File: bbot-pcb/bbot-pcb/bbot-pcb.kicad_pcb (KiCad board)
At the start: 2 copper layers, 72.4 x 56.5 mm, 12 parts, among them U1 HA-552-4P, U2 ADXL335, U3 HA-552-4P, U4 OPENLOG

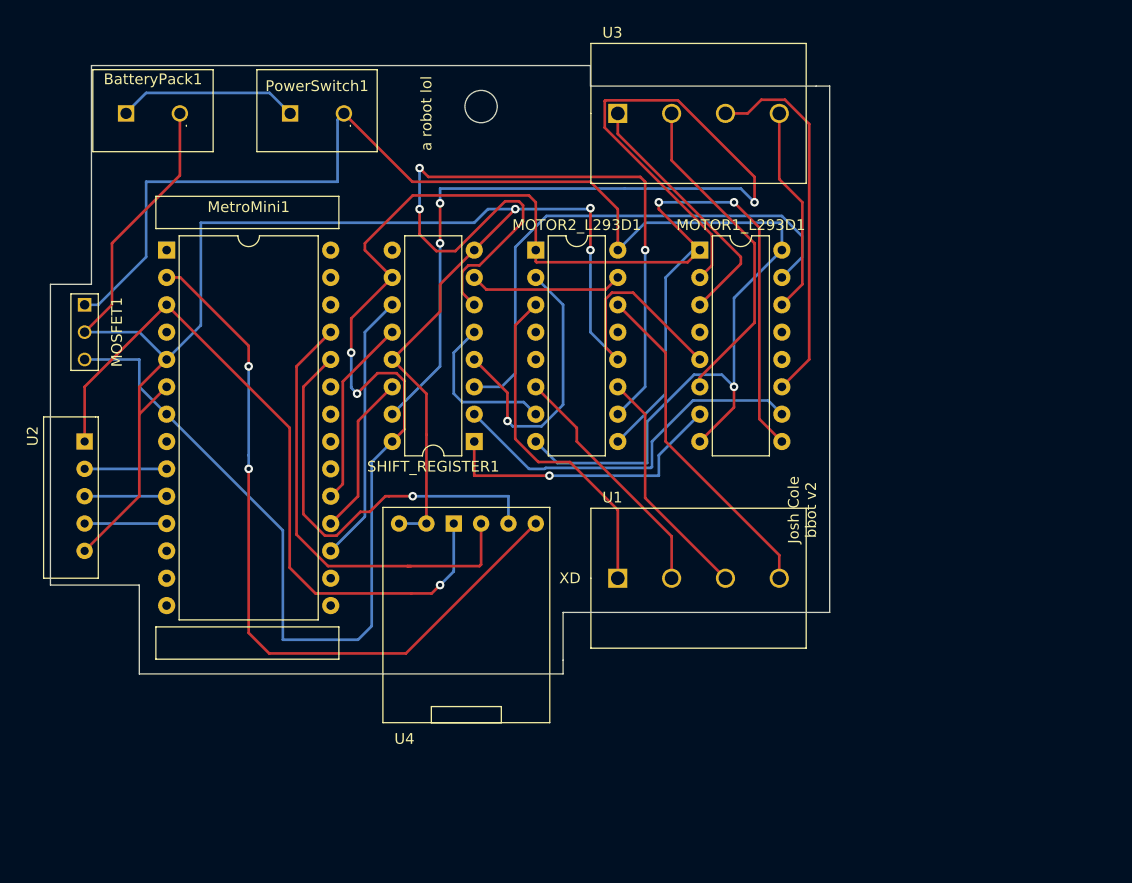
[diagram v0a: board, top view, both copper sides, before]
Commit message: Update PCB to v3
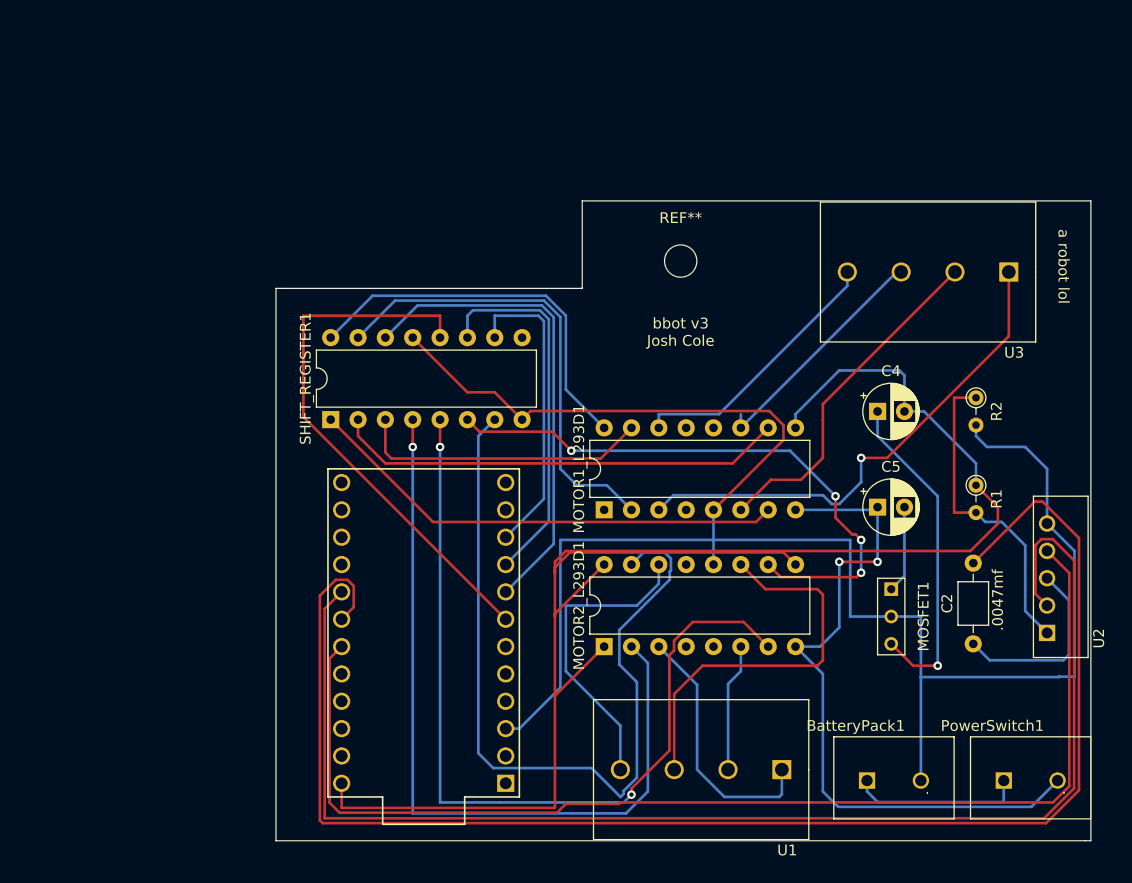
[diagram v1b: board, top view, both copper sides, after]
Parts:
- removed MetroMini1: MetroMini, Package_DIP:DIP-28_W15.24mm
- added C2: C.0047mf, Capacitor_THT:C_Axial_L3.8mm_D2.6mm_P7.50mm_Horizontal, F.Cu at (229.9, 72.1)
- added C4: L7805_OUT_CAP, Capacitor_THT:CP_Radial_D5.0mm_P2.50mm, F.Cu at (221.0, 50.5)
- added C5: L7805_IN_CAP, Capacitor_THT:CP_Radial_D5.0mm_P2.50mm, F.Cu at (221.0, 59.4)
- added R1: SPARKFUN-RESISTORS_4.7KOHM-0603-1_10W-1%, Resistor_THT:R_Axial_DIN0204_L3.6mm_D1.6mm_P2.54mm_Vertical, F.Cu at (230.1, 57.4)
- added R2: SPARKFUN-RESISTORS_4.7KOHM-0603-1_10W-1%, Resistor_THT:R_Axial_DIN0204_L3.6mm_D1.6mm_P2.54mm_Vertical, F.Cu at (230.1, 49.3)
- U4: value OPENLOG -> ArduinoProMicro; footprint bbot-pcb:OPENLOG -> promicro:ProMicro
- moved BatteryPack1 92.6 mm to (222.5, 84.8)
- moved U2 91.2 mm to (236.7, 71.1), turned to 90 degrees
- moved PowerSwitch1 90.8 mm to (235.2, 84.8)
- moved MOSFET1 79.5 mm to (222.2, 69.6)
- moved U3 39.2 mm to (233.2, 37.6), turned to 180 degrees
- moved MOTOR2_L293D1 37.4 mm to (195.6, 72.4), turned to 90 degrees
- moved MOTOR1_L293D1 25.7 mm to (195.6, 59.7), turned to 90 degrees
- moved REF** 23.4 mm to (202.7, 36.6)
- moved U1 23.4 mm to (212.1, 83.8), turned to 180 degrees
- moved SHIFT_REGISTER1 13.5 mm to (170.2, 51.3), turned to 90 degrees
- moved U4 10.4 mm to (178.8, 71.1), turned to 90 degrees
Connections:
- BatteryPack1 pad 2: GND -> /GND
- MOSFET1 pad 1: /12V -> Net-(C5-Pad2)
- MOSFET1 pad 2: GND -> /GND
- MOSFET1 pad 3: 5V -> Net-(C4-Pad1)
- MOTOR1_L293D1 pad 1: 5V -> /5V
- MOTOR1_L293D1 pad 16: /12V -> /5V
- MOTOR1_L293D1 pad 5: GND -> /GND
- MOTOR1_L293D1 pad 9: 5V -> /5V
- MOTOR2_L293D1 pad 1: 5V -> /5V
- MOTOR2_L293D1 pad 12: GND -> /GND
- MOTOR2_L293D1 pad 16: /12V -> /5V
- MOTOR2_L293D1 pad 9: 5V -> /5V
- SHIFT_REGISTER1 pad 10: 5V -> /SHIFT_CLR
- SHIFT_REGISTER1 pad 11: SHIFT_CLCK -> /SHIFT_CLCK
- SHIFT_REGISTER1 pad 12: SHIFT_LATCH -> /SHIFT_LATCH
- SHIFT_REGISTER1 pad 13: GND -> /GND
- SHIFT_REGISTER1 pad 14: SHIFT_DATA -> /SHIFT_DATA
- SHIFT_REGISTER1 pad 16: 5V -> /5V
- SHIFT_REGISTER1 pad 8: GND -> /GND
- U2 pad 3: /A1 -> Net-(C2-Pad1)
- U2 pad 5: GND -> /GND
- U4 pad 1: GND -> Net-(U4-Pad1)
- U4 pad 2: GND -> Net-(U4-Pad2)
- U4 pad 3: /3V -> /GND
- U4 pad 4: /TX -> Net-(U4-Pad4)
- U4 pad 5: /RX -> Net-(U4-Pad5)
- U4 pad 6: /RST -> Net-(U4-Pad6)
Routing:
- net /5V: track 0.00 -> 192.5 mm
- net 5V: track 189.3 -> 0.00 mm, vias 4 -> 0
- net GND: track 178.6 -> 0.00 mm, vias 3 -> 0
- net /GND: track 0.00 -> 173.8 mm
- net /A1: track 7.62 -> 137.3 mm
- net /A0: track 7.62 -> 124.3 mm
- net /A2: track 7.62 -> 107.8 mm
- net /12V: track 137.0 -> 65.2 mm, vias 1 -> 2
- net /RST: track 69.4 -> 0.00 mm, vias 2 -> 0
- net /MOTOR2_B: track 14.9 -> 80.0 mm, vias 0 -> 2
- net /MOTOR2_D: track 14.3 -> 76.3 mm
- net /SHIFT_LATCH: track 0.00 -> 50.7 mm
- net /MOTOR1_A: track 92.9 -> 43.1 mm, vias 3 -> 0
- net /MOTOR2_A: track 26.1 -> 73.4 mm
- net /SHIFT_DATA: track 0.00 -> 44.7 mm
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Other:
- board size 72.4 x 56.5 mm -> 75.7 x 59.4 mm
- board text added: ".0047mf"
- board text added: "bbot v3 Josh Cole"
- board text removed: "Josh Cole bbot v2"

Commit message: RElease-candidate of models and pcb
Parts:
- removed REF**: MountingHole_3mm, MountingHole:MountingHole_3mm
- added Mounting Hole: MountingHole_3mm, MountingHole:MountingHole_3mm, F.Cu at (204.7, 36.6)
- C4, C5: footprint Capacitor_THT:CP_Radial_D5.0mm_P2.50mm -> Capacitor_THT:C_Disc_D4.3mm_W1.9mm_P5.00mm
- moved SHIFT_REGISTER1 19.1 mm to (187.5, 43.2), turned to 270 degrees
- moved C4 2.05 mm to (220.0, 52.3)
- moved C5 1.14 mm to (220.0, 58.9)
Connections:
- U4 pad 10: /SHIFT_CLR -> /SHIFT_DATA
- U4 pad 7: /SHIFT_LATCH -> /SHIFT_CLR
- U4 pad 8: /SHIFT_DATA -> /SHIFT_CLCK
- U4 pad 9: /SHIFT_CLCK -> /SHIFT_LATCH
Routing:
- net /5V: track 192.5 -> 135.1 mm, vias 0 -> 1
- net /MOTOR2_D: track 76.3 -> 38.5 mm
- net /SHIFT_LATCH: track 50.7 -> 17.8 mm
- net /MOTOR2_A: track 73.4 -> 41.7 mm
- net /SHIFT_DATA: track 44.7 -> 13.1 mm
- net /GND: track 173.8 -> 194.6 mm, vias 0 -> 1
- net /MOTOR2_B: track 80.0 -> 61.1 mm, vias 2 -> 1
- net /MOTOR2_PHASE_C: track 37.0 -> 22.9 mm
- net /SHIFT_CLCK: track 34.6 -> 21.3 mm
- net /MOTOR1_A: track 43.1 -> 54.9 mm, vias 0 -> 1
- net /MOTOR1_C: track 42.0 -> 32.5 mm
- net /MOTOR2_PHASE_D: track 28.6 -> 20.6 mm
- net /MOTOR1_D: track 27.3 -> 19.4 mm
- net Net-(C4-Pad1): track 31.4 -> 24.4 mm, vias 1 -> 0
- net /MOTOR1_B: track 45.0 -> 38.6 mm
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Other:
- net class Default: trace_width 0.25 -> 0.2
- rule trace_min: 0.2 -> 0.127
- board text added: "0.1mf"
- board text added: "0.33mf"
- board text added: "bbot v4 Josh Cole"
- board text removed: "bbot v3 Josh Cole"
